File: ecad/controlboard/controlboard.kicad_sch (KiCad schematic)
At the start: 34 parts, among them J1 B6B-XH-A(LF)(SN), SW1 KSC_SLT_241G_LFS

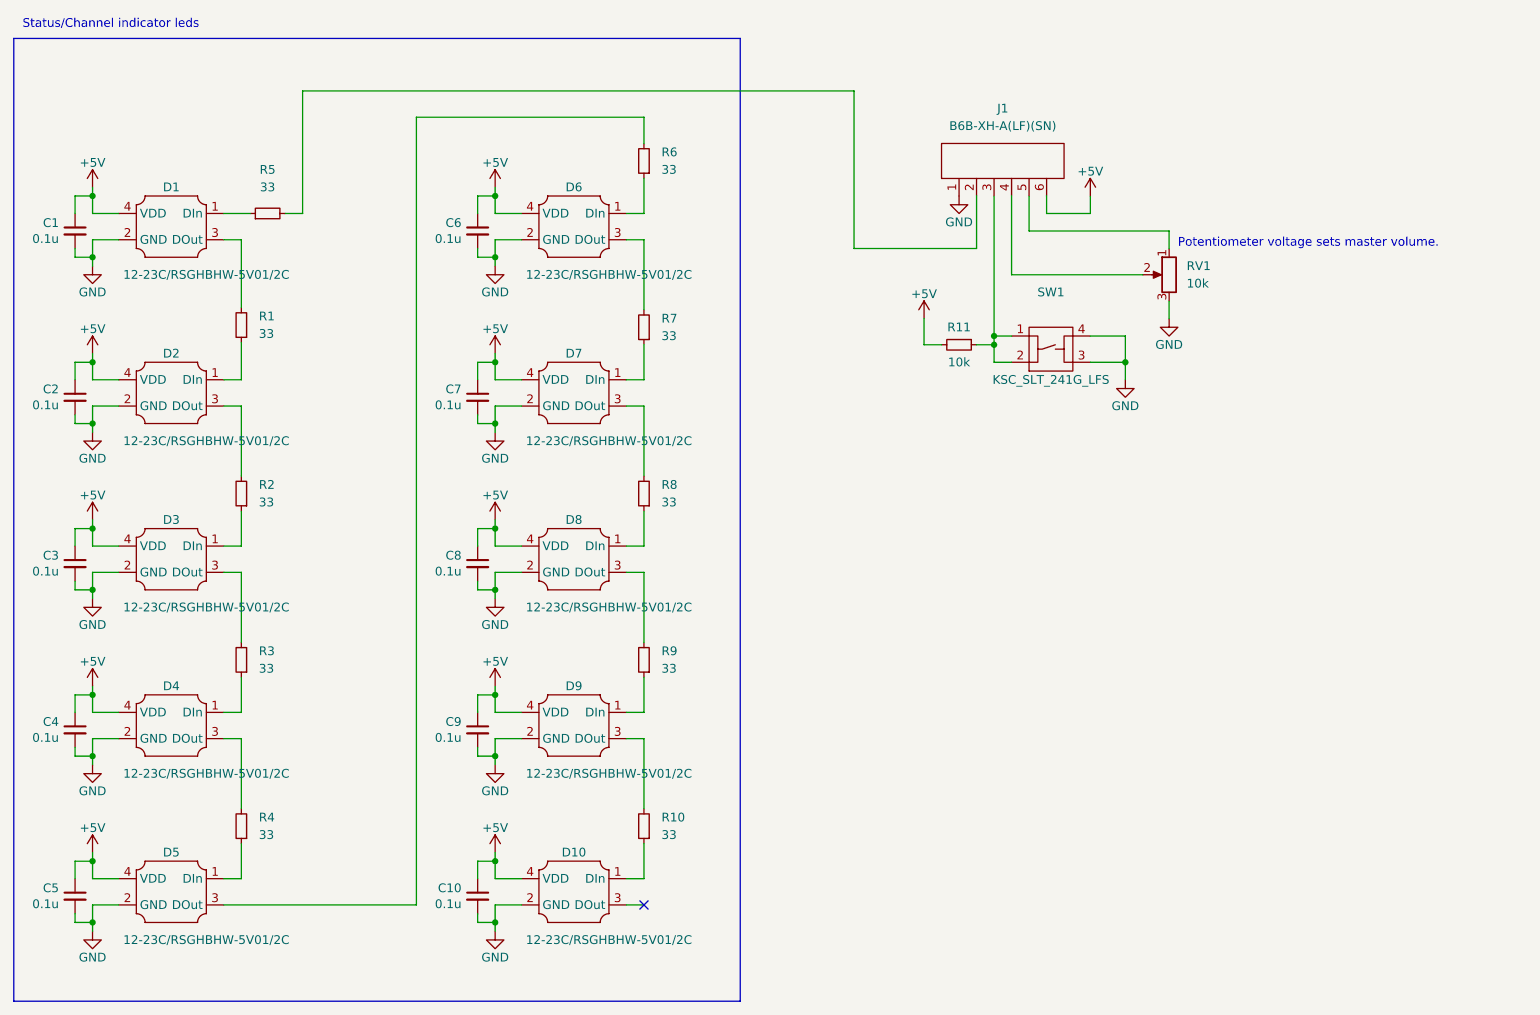
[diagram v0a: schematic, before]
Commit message: Change addressable LED to new part that is still available.
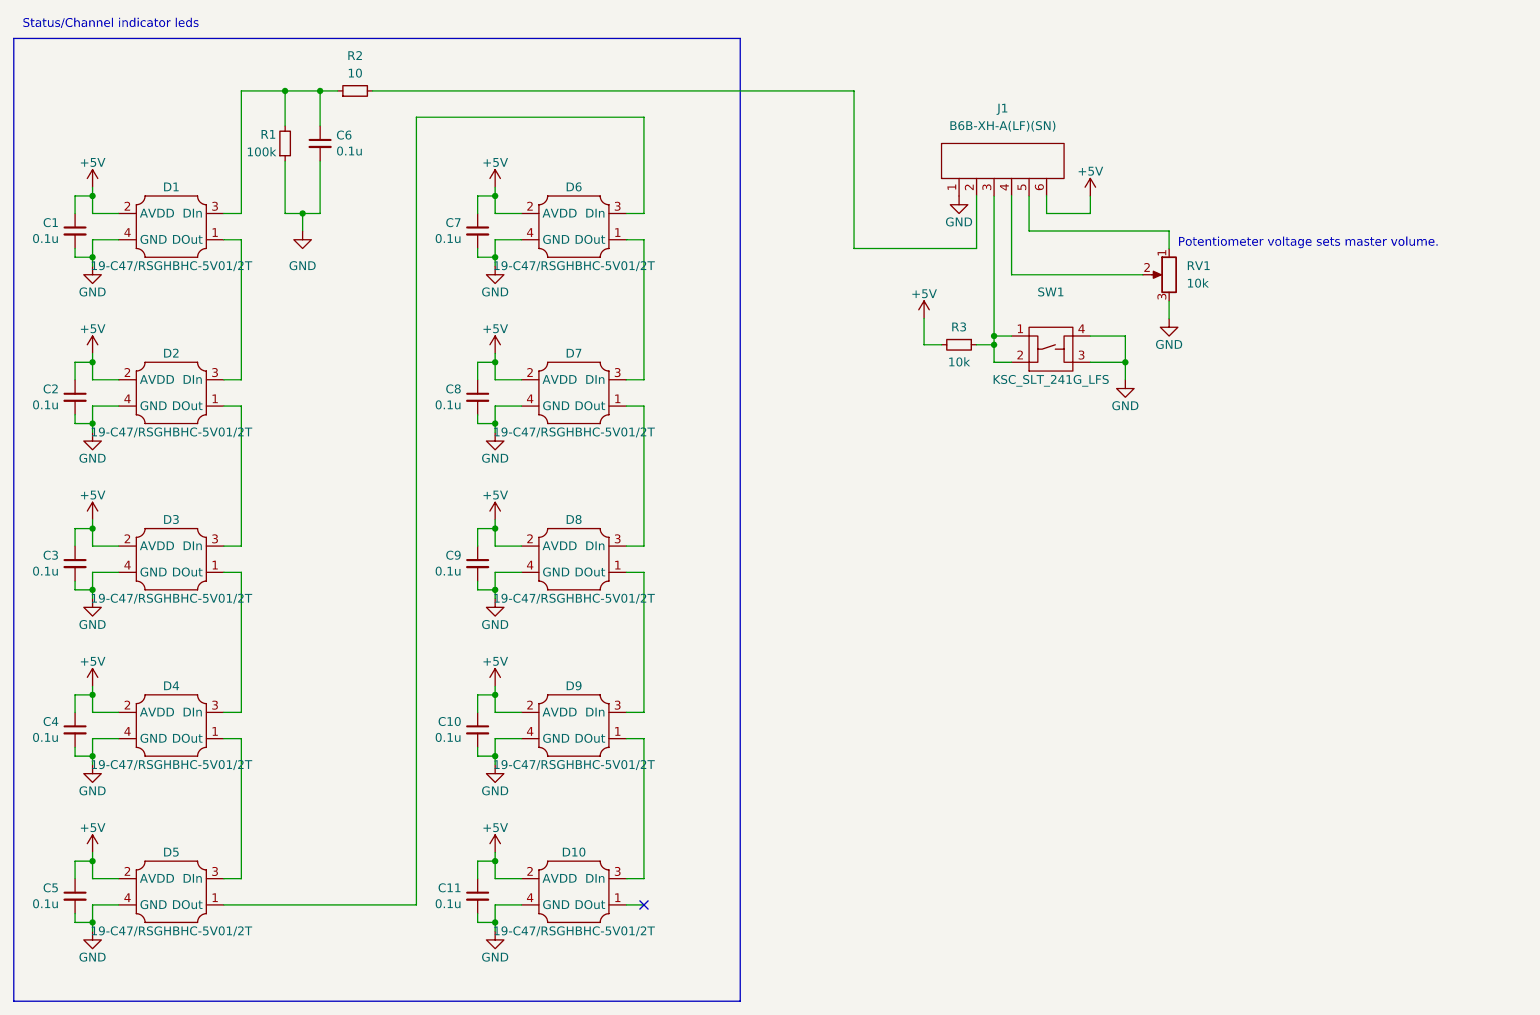
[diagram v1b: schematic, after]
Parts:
- removed R1, R10, R3, R4, R6, R7, R8, R9: 33, Resistor_SMD:R_0603_1608Metric_Pad0.98x0.95mm_HandSolder, symbol Device:R_Small
- added C6: 0.1u, Capacitor_SMD:C_0603_1608Metric_Pad1.08x0.95mm_HandSolder, symbol Device:C_Small
- D1, D10, D2, D3, D4, D5, D6, D7, D8, D9: value 12-23C/RSGHBHW-5V01/2C -> 19-C47/RSGHBHC-5V01/2T; footprint silver-box-feetprints:12-23C-RSGHBHW-5V01-2C -> silver-box-feetprints:19-C47 RSGHBHC-5V01 2T; symbol silver-box-modular:12-23C/RSGHBHW-5V01/2C -> silver-box-modular:19-C47/RSGHBHC-5V01/2T
- R1: renamed from R5; value 33 -> 100k
- R2: value 33 -> 10
- renumbered C9 to C10, C10 to C11, C6 to C7, C7 to C8, C8 to C9, R11 to R3
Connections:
- net +5V: now also D1.2 (AVDD), D10.2 (AVDD), D2.2 (AVDD), D3.2 (AVDD), D4.2 (AVDD), D5.2 (AVDD), D6.2 (AVDD), D7.2 (AVDD), D8.2 (AVDD), D9.2 (AVDD); no longer D1.4 (VDD), D10.4 (VDD), D2.4 (VDD), D3.4 (VDD), D4.4 (VDD), D5.4 (VDD), D6.4 (VDD), D7.4 (VDD), D8.4 (VDD), D9.4 (VDD)
- net GND: now also D1.4 (GND), D10.4 (GND), D2.4 (GND), D3.4 (GND), D4.4 (GND), D5.4 (GND), D6.4 (GND), D7.4 (GND), D8.4 (GND), D9.4 (GND), R1.1, C6.2; no longer D1.2 (GND), D10.2 (GND), D2.2 (GND), D3.2 (GND), D4.2 (GND), D5.2 (GND), D6.2 (GND), D7.2 (GND), D8.2 (GND), D9.2 (GND)
- net at D7.1 (DOut): now also D8.3 (DIn)
- net at D7.3 (DIn): now also D6.1 (DOut)
- net at D6.3 (DIn): now also D5.1 (DOut)
- net at D9.1 (DOut): now also D10.3 (DIn)
- net at D9.3 (DIn): now also D8.1 (DOut)
- net at D1.1 (DOut): now also D2.3 (DIn); no longer R1.1
- net at R1.2: now also D1.3 (DIn), R2.1, C6.1; no longer J1.2
- net at D3.1 (DOut): now also D4.3 (DIn); no longer R2.1
- net at D3.3 (DIn): now also D2.1 (DOut)
- net at R2.2: now also J1.2; no longer D2.3 (DOut)
- net at D4.1 (DOut): now also D5.3 (DIn)
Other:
- moved on the sheet: R1
